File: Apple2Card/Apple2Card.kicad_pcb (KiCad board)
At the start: 2 copper layers, 160 x 78.2 mm, 57 parts, among them J2 Conn_01x25, J3 Conn_01x25, U2 74HCT32, U3 74HCT00, U4 82C55A, U9 28C256

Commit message: JLCPCB Order 2022-06-15
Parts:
- added J1: Conn_01x02, Connector_PinSocket_2.54mm:PinSocket_1x02_P2.54mm_Vertical, F.Cu at (55.0, 85.0)
- added R33: 1k, Resistor_THT:R_Axial_DIN0207_L6.3mm_D2.5mm_P7.62mm_Horizontal, B.Cu at (51.1, 59.4)
- added R34: 1k, Resistor_THT:R_Axial_DIN0207_L6.3mm_D2.5mm_P7.62mm_Horizontal, B.Cu at (50.9, 69.8)
- moved C1 8.25 mm to (51.7, 79.6), turned to 90 degrees
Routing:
- net PC1: track 139.0 -> 183.6 mm
- net Net-(J1-Pad1): track 0.00 -> 31.5 mm
- net PC0: track 127.8 -> 157.5 mm
- net Net-(J1-Pad2): track 0.00 -> 26.2 mm
- net Net-(A1-Pad23): track 111.4 -> 121.2 mm
- net Net-(A1-Pad27): track 119.6 -> 129.4 mm
- net Net-(A1-Pad30): track 9.06 -> 18.5 mm

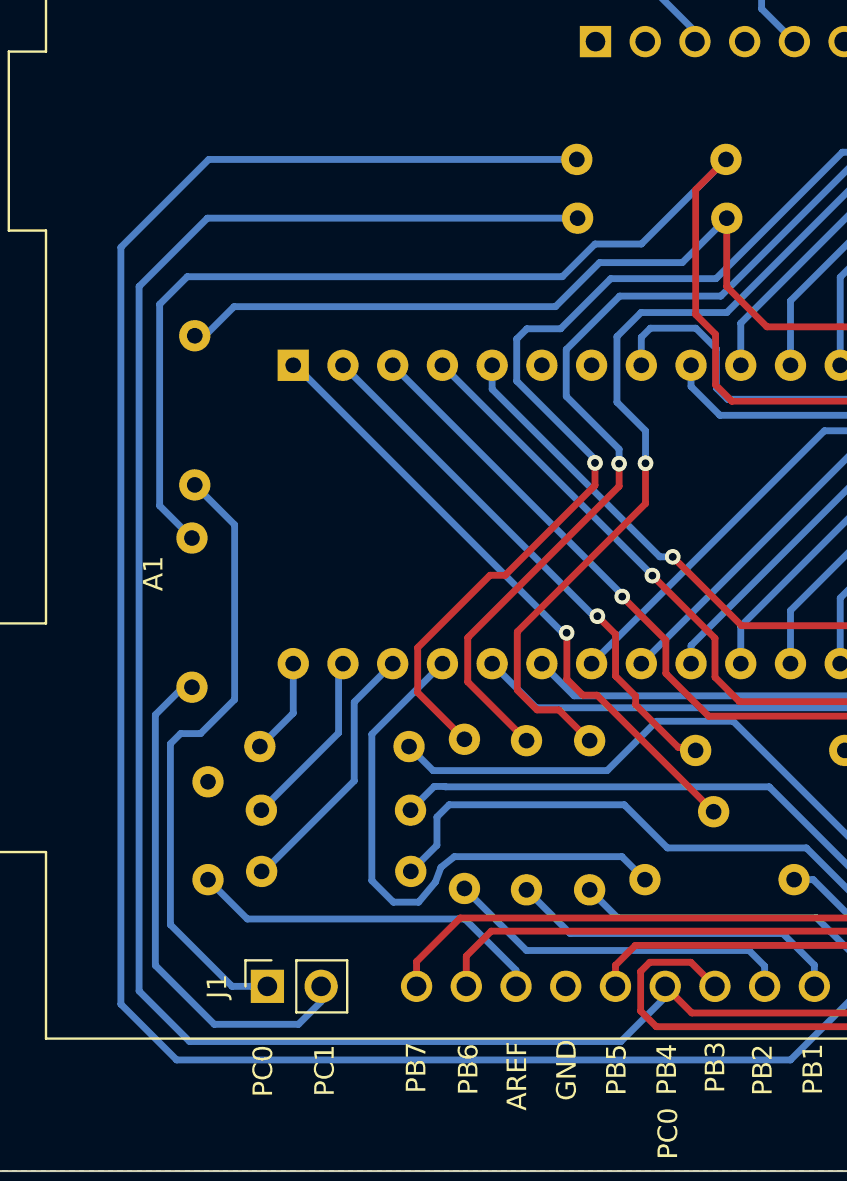
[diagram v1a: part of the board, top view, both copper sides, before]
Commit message: Fixed layout a bit, added pictures
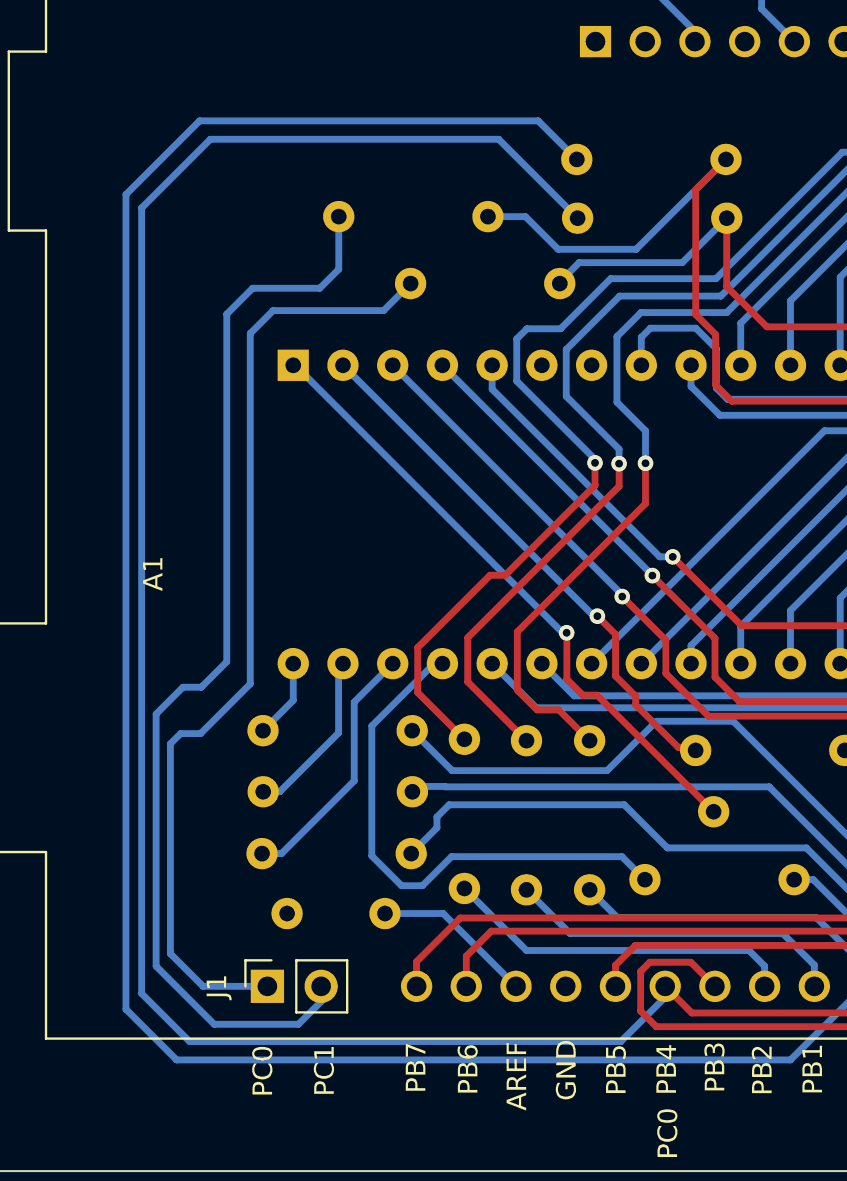
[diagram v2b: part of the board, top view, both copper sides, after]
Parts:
- moved R34 25.2 mm to (58.4, 45.7), turned to 0 degrees
- moved R33 15.1 mm to (62.1, 49.1), turned to 0 degrees
- moved C1 9.20 mm to (60.8, 81.3), turned to 180 degrees
- moved R6 0.94 mm to (62.2, 75.1)
- moved R15 0.91 mm to (62.1, 78.3)
- moved R14 0.83 mm to (62.2, 72.0)
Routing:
- net PC1: track 183.6 -> 153.7 mm
- net Net-(J1-Pad2): track 26.2 -> 55.6 mm
- net PC0: track 157.5 -> 137.8 mm
- net Net-(J1-Pad1): track 31.5 -> 48.9 mm
- net Net-(A1-Pad30): track 18.5 -> 8.24 mm
- net Net-(A1-Pad27): track 129.4 -> 134.9 mm
- net Net-(A1-Pad23): track 121.2 -> 124.1 mm
- net PA7: track 28.7 -> 27.2 mm
- net Net-(A1-Pad21): track 36.4 -> 35.5 mm
- net PA4: track 4.94 -> 4.06 mm
